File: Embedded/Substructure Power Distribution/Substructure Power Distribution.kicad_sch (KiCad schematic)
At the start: 1 part, among them J1 S JST

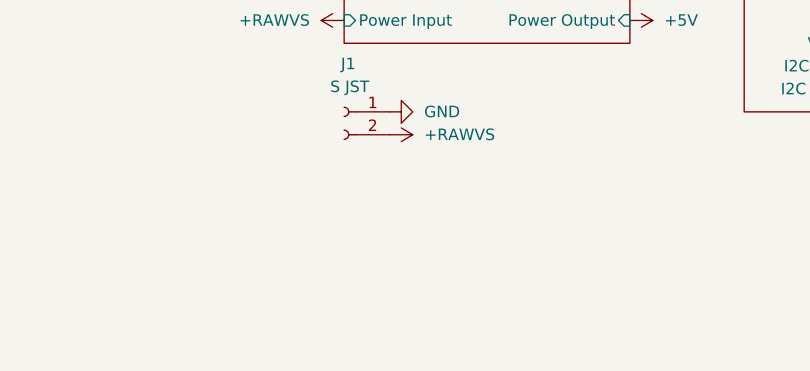
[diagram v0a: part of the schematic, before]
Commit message: Added Display Power Connectors (Migrated from Snoot)
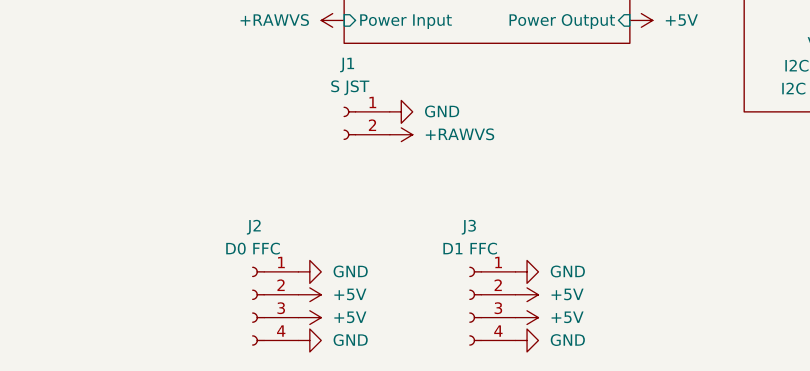
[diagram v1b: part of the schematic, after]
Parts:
- added J2: D0 FFC, Connector_JST:JST_XH_B4B-XH-A_1x04_P2.50mm_Vertical, symbol Connector:Conn_01x04_Socket
- added J3: D1 FFC, Connector_JST:JST_XH_B4B-XH-A_1x04_P2.50mm_Vertical, symbol Connector:Conn_01x04_Socket
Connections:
- net +5V: now also J2.2 (Pin_2), J2.3 (Pin_3), J3.2 (Pin_2), J3.3 (Pin_3)
- net GND: now also J2.1 (Pin_1), J2.4 (Pin_4), J3.1 (Pin_1), J3.4 (Pin_4)

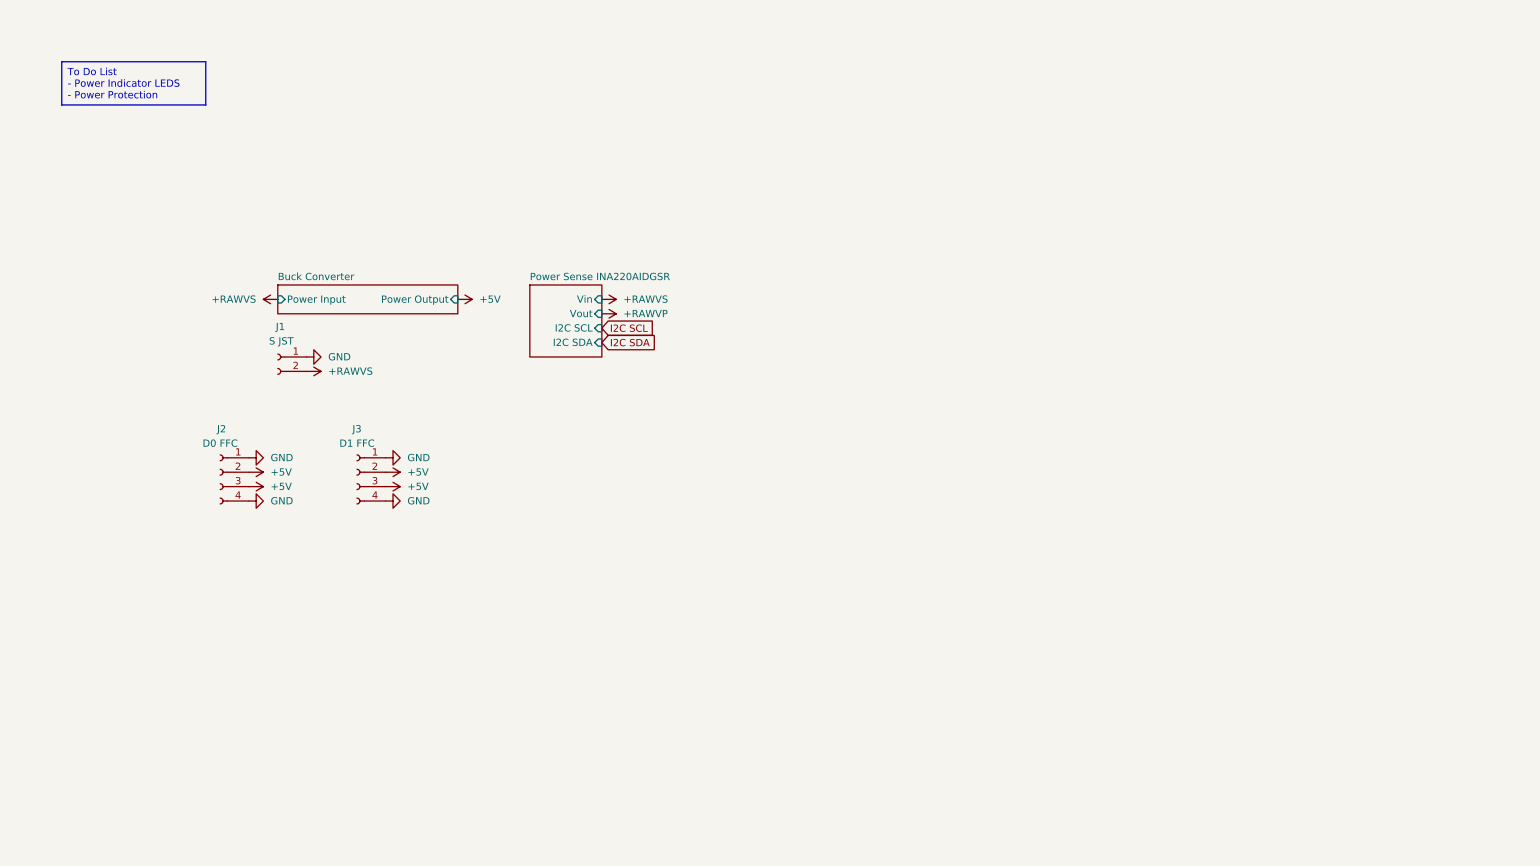
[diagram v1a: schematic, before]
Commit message: Added Protection & LED Indicators List
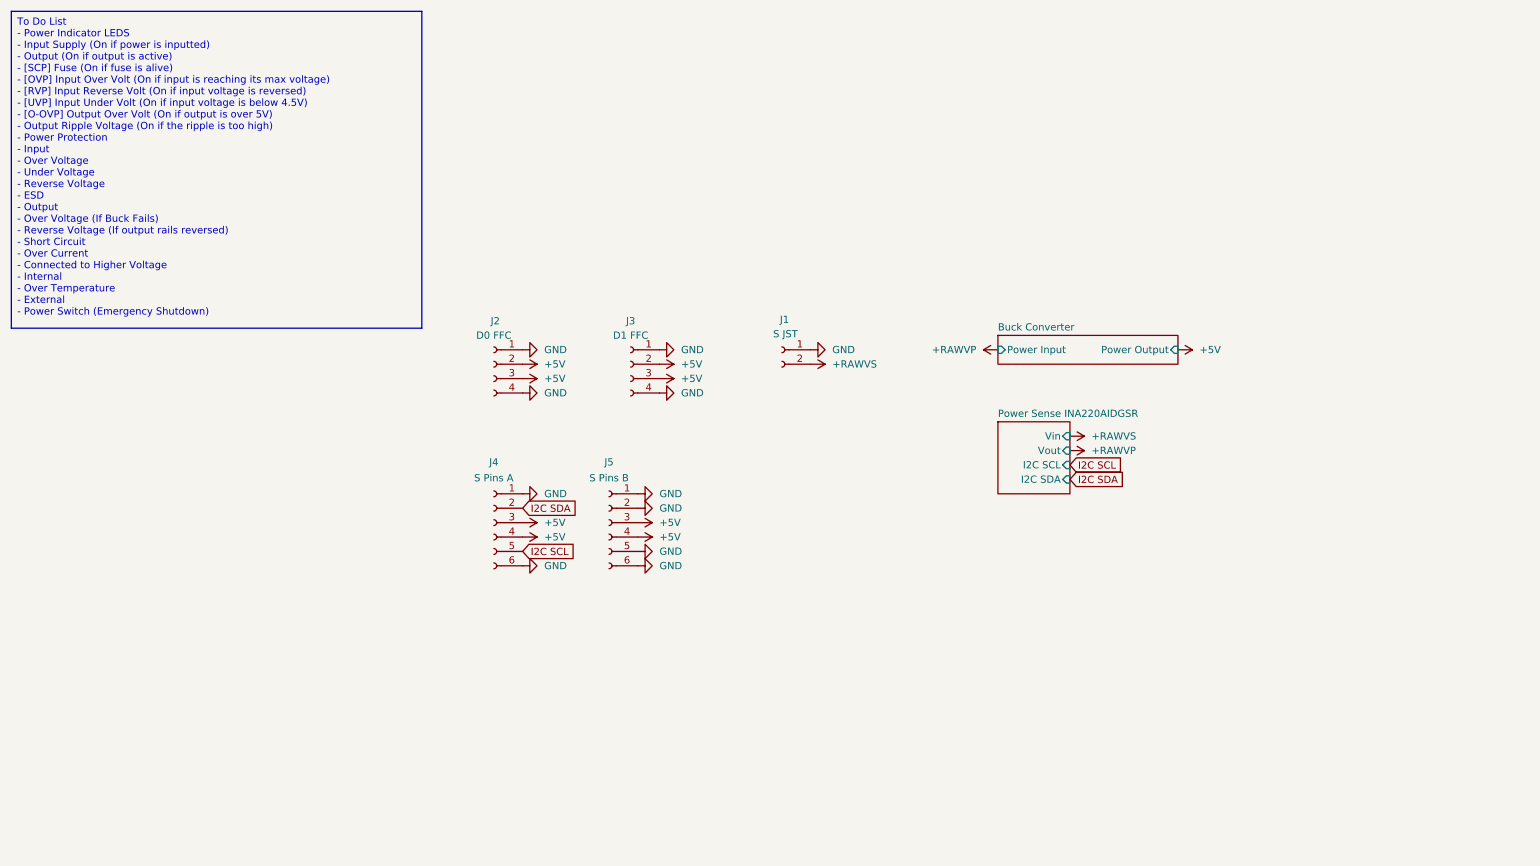
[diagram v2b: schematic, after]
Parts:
- added J4: S Pins A, Connector_PinHeader_2.54mm:PinHeader_1x06_P2.54mm_Vertical, symbol Connector:Conn_01x06_Socket
- added J5: S Pins B, Connector_PinHeader_2.54mm:PinHeader_1x06_P2.54mm_Vertical, symbol Connector:Conn_01x06_Socket
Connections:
- net +5V: now also J4.3 (Pin_3), J4.4 (Pin_4), J5.3 (Pin_3), J5.4 (Pin_4)
- net GND: now also J4.1 (Pin_1), J4.6 (Pin_6), J5.1 (Pin_1), J5.2 (Pin_2), J5.5 (Pin_5), J5.6 (Pin_6)
- net I2C SCL: now also J4.5 (Pin_5)
- net I2C SDA: now also J4.2 (Pin_2)
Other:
- moved on the sheet: J1, J2, J3

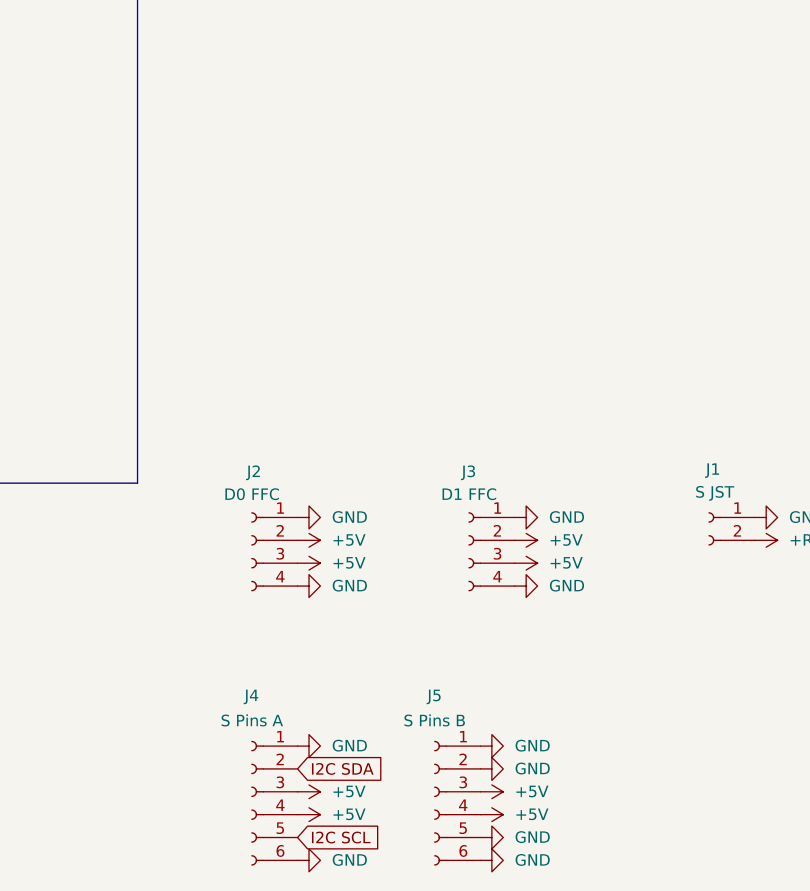
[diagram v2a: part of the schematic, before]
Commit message: Added Enable Pins to PSU Connector
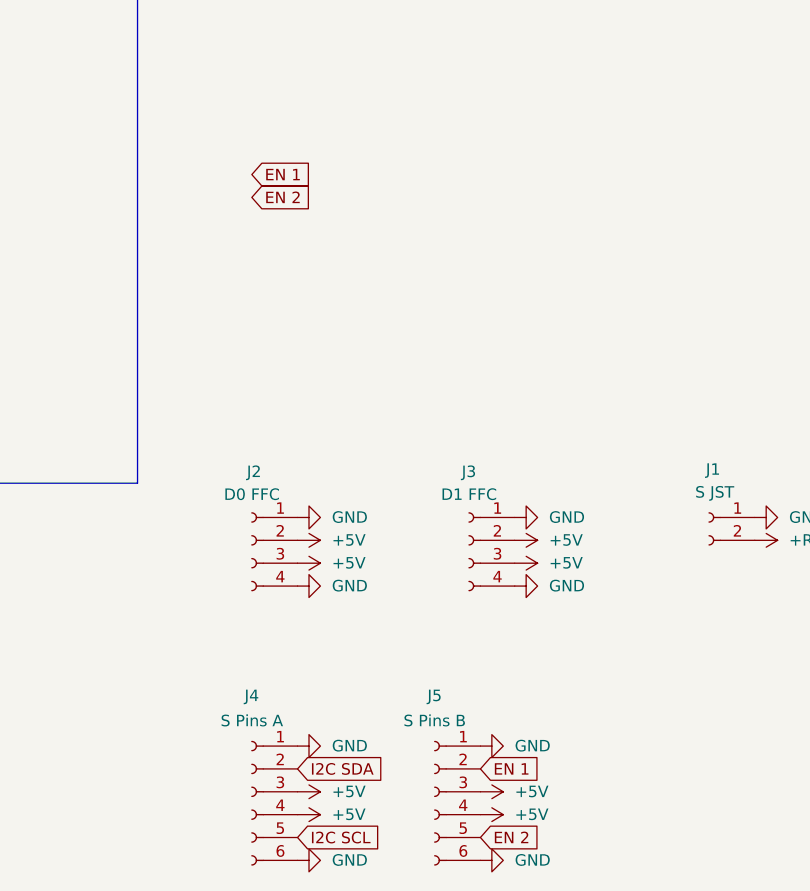
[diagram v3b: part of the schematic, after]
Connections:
- net GND: no longer J5.2 (Pin_2), J5.5 (Pin_5)
- new net EN 1: J5.2 (Pin_2)
- new net EN 2: J5.5 (Pin_5)
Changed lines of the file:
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@@
+		)
+	)
+	(global_label "EN 2"
+		(shape input)
+		(at 101.6 40.64 0)
+		(fields_autoplaced yes)
+		(effects
+			(font
+				(size 1.27 1.27)
+			)
+			(justify left)
+		)
+		(property "Intersheetrefs" "${INTERSHEET_REFS}"
+			(at 109.2418 40.64 0)
+			(effects
+				(font
+					(size 1.27 1.27)
+				)
+				(justify left)
+				(hide yes)
+			)
 		)
 	)
@@
 		)
 	)
+	(global_label "EN 1"
+		(shape input)
+		(at 127 104.14 0)
+		(fields_autoplaced yes)
+		(effects
+			(font
+				(size 1.27 1.27)
+			)
+			(justify left)
+		)
+		(property "Intersheetrefs" "${INTERSHEET_REFS}"
+			(at 134.6418 104.14 0)
+			(effects
+				(font
+					(size 1.27 1.27)
+				)
+				(justify left)
+				(hide yes)
+			)
+		)
+	)
 	(global_label "I2C SDA"
 		(shape input)
@@
 		)
 	)
+	(global_label "EN 2"
+		(shape input)
+		(at 127 111.76 0)
+		(fields_autoplaced yes)
+		(effects
+			(font
+				(size 1.27 1.27)
+			)
+			(justify left)
+		)
+		(property "Intersheetrefs" "${INTERSHEET_REFS}"
+			(at 134.6418 111.76 0)
+			(effects
+				(font
+					(size 1.27 1.27)
+				)
+				(justify left)
+				(hide yes)
+			)
+		)
+	)
+	(global_label "EN 1"
+		(shape input)
+		(at 101.6 38.1 0)
+		(fields_autoplaced yes)
+		(effects
+			(font
+				(size 1.27 1.27)
+			)
+			(justify left)
+		)
+		(property "Intersheetrefs" "${INTERSHEET_REFS}"
+			(at 109.2418 38.1 0)
+			(effects
+				(font
+					(size 1.27 1.27)
+				)
+				(justify left)
+				(hide yes)
+			)
+		)
+	)
 	(symbol
 		(lib_id "power:+5VP")
@@
 				(path "/6e7c3700-4b7d-4b10-b755-ccb609125a98"
 					(reference "#PWR05")
-					(unit 1)
-				)
-			)
-		)
-	)
-	(symbol
-		(lib_id "power:GND")
-		(at 127 111.76 90)
-		(unit 1)
-		(exclude_from_sim no)
-		(in_bom yes)
-		(on_board yes)
-		(dnp no)
-		(fields_autoplaced yes)
-		(property "Reference" "#PWR039"
-			(at 133.35 111.76 0)
-			(effects
-				(font
-					(size 1.27 1.27)
-				)
-				(hide yes)
-			)
-		)
-		(property "Value" "GND"
-			(at 130.81 111.7599 90)
-			(effects
-				(font
-					(size 1.27 1.27)
-				)
-				(justify right)
-			)
-		)
-		(property "Footprint" ""
-			(at 127 111.76 0)
-			(effects
-				(font
-					(size 1.27 1.27)
-				)
-				(hide yes)
-			)
-		)
-		(property "Datasheet" ""
-			(at 127 111.76 0)
-			(effects
-				(font
-					(size 1.27 1.27)
-				)
-				(hide yes)
-			)
-		)
-		(property "Description" "Power symbol creates a global label with name \"GND\" , ground"
-			(at 127 111.76 0)
-			(effects
-				(font
-					(size 1.27 1.27)
-				)
-				(hide yes)
-			)
-		)
-		(pin "1"
-		)
-		(instances
-			(project "Substructure Power Distribution"
-				(path "/6e7c3700-4b7d-4b10-b755-ccb609125a98"
-					(reference "#PWR039")
 					(unit 1)
 				)
@@
 					(unit 1)
 				)
-			)
-		)
-	)
-	(symbol
-		(lib_id "power:GND")
-		(at 127 104.14 90)
-		(unit 1)
-		(exclude_from_sim no)
-		(in_bom yes)
-		(on_board yes)
-		(dnp no)
-		(fields_autoplaced yes)
-		(property "Reference" "#PWR036"
-			(at 133.35 104.14 0)
-			(effects
-				(font
-					(size 1.27 1.27)
-				)
-				(hide yes)
-			)
-		)
-		(property "Value" "GND"
-			(at 130.81 104.1399 90)
-			(effects
-				(font
-					(size 1.27 1.27)
-				)
-				(justify right)
-			)
-		)
-		(property "Footprint" ""
-			(at 127 104.14 0)
-			(effects
-				(font
-					(size 1.27 1.27)
-				)
-				(hide yes)
-			)
-		)
-		(property "Datasheet" ""
-			(at 127 104.14 0)
-			(effects
-				(font
-					(size 1.27 1.27)
-				)
-				(hide yes)
-			)
-		)
-		(property "Description" "Power symbol creates a global label with name \"GND\" , ground"
-			(at 127 104.14 0)
-			(effects
-				(font
-					(size 1.27 1.27)
-				)
-				(hide yes)
-			)
-		)
-		(pin "1"
-		)
-		(instances
-			(project "Substructure Power Distribution"
-				(path "/6e7c3700-4b7d-4b10-b755-ccb609125a98"
-					(reference "#PWR036")
-					(unit 1)
-				)

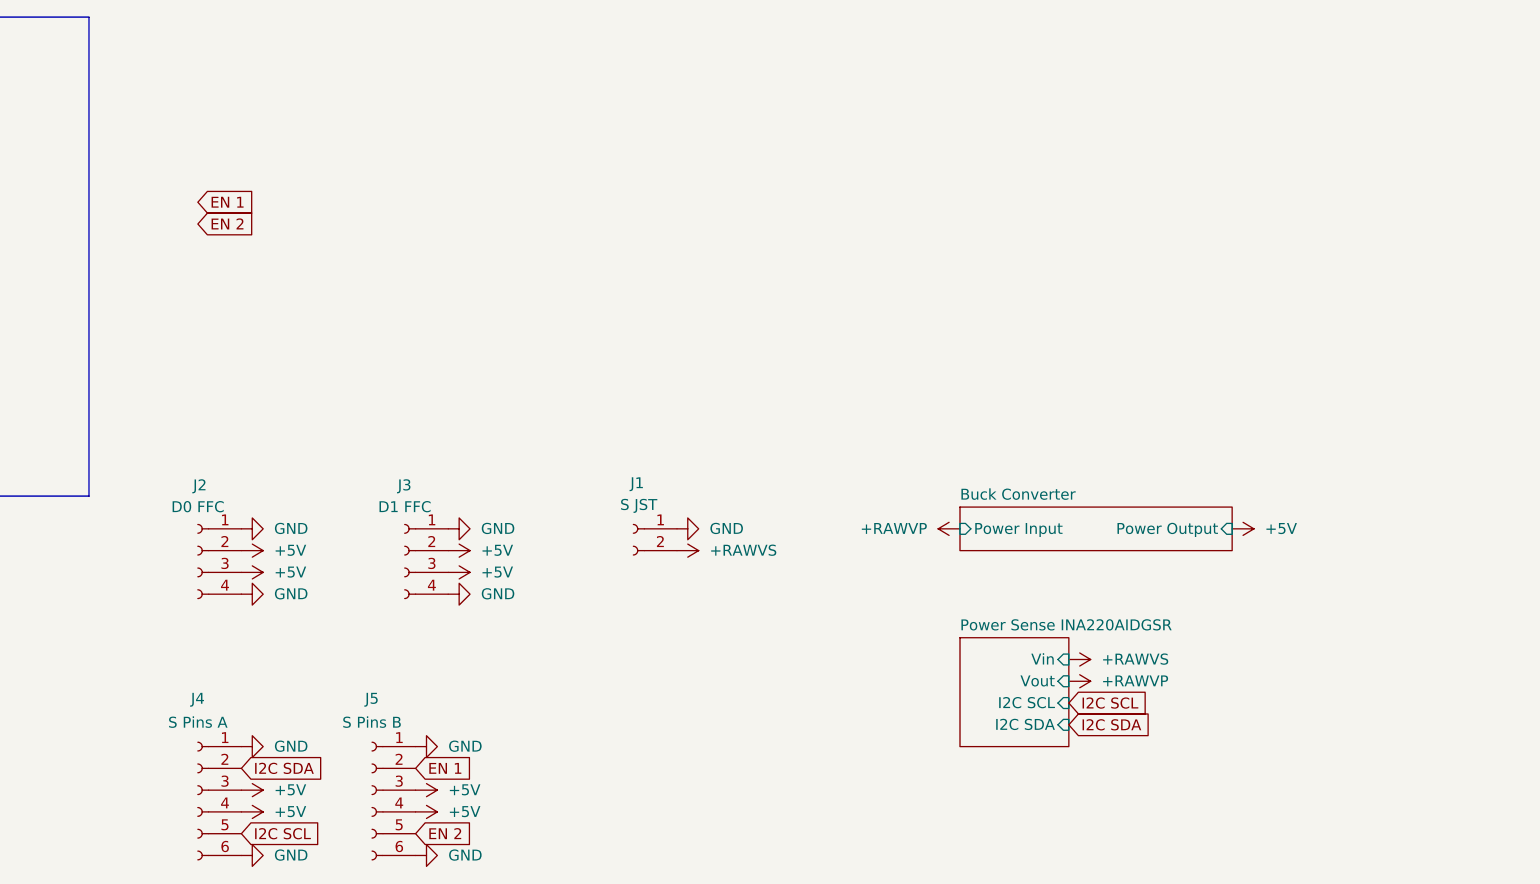
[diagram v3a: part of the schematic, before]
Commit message: Added Mill Max Connectors
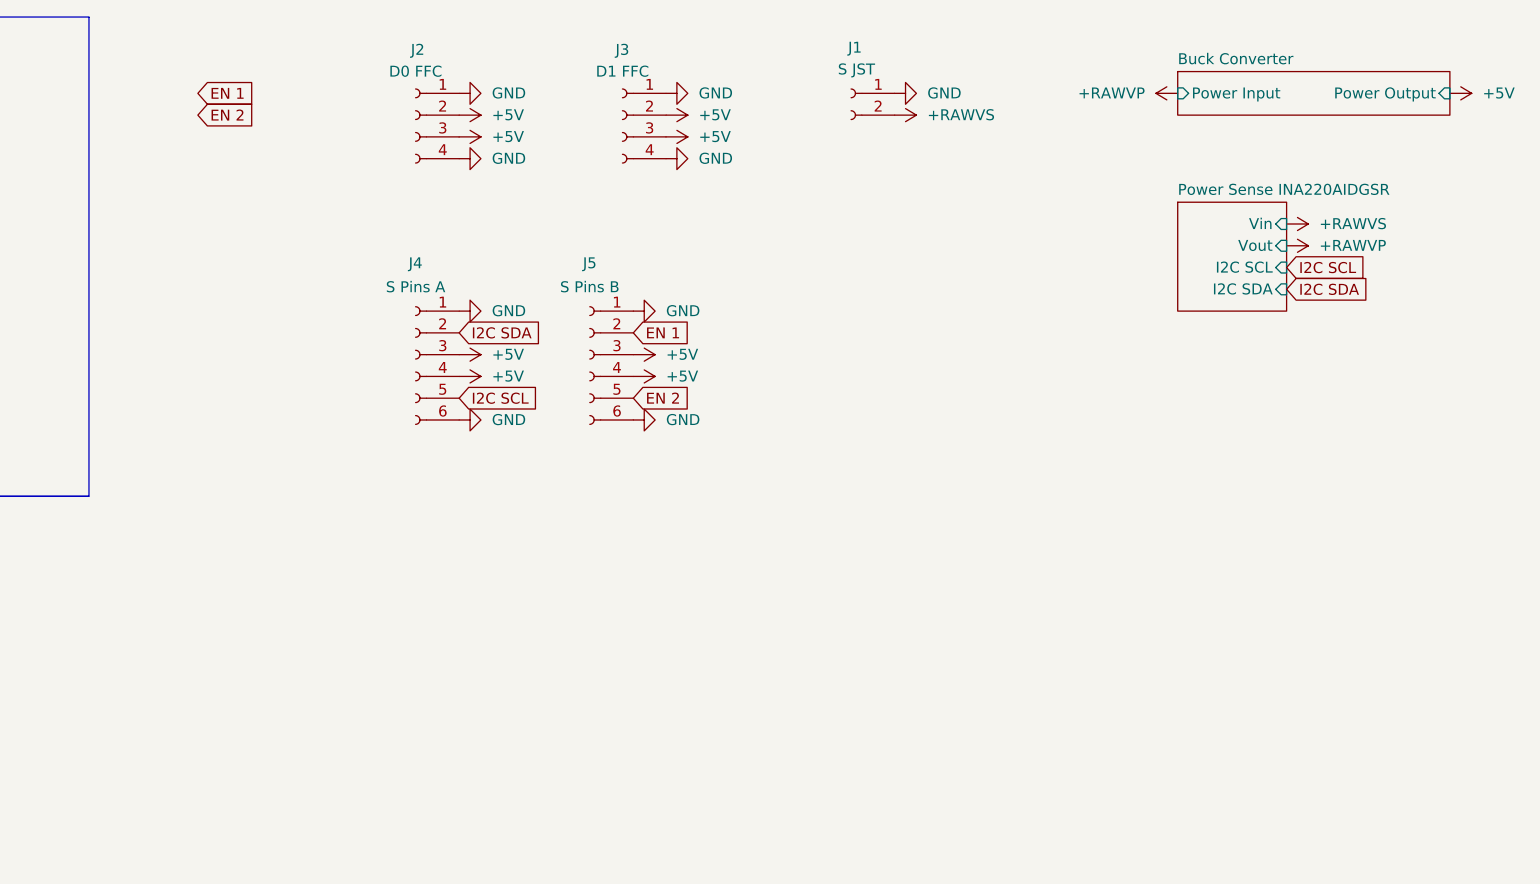
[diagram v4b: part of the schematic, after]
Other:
- moved on the sheet: J1, J2, J3, J4, J5
